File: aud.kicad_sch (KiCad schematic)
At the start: 17 parts, among them J1 AudioJack3_Ground, J3 Conn_01x12_Socket, U1 XTAD5212IRGER

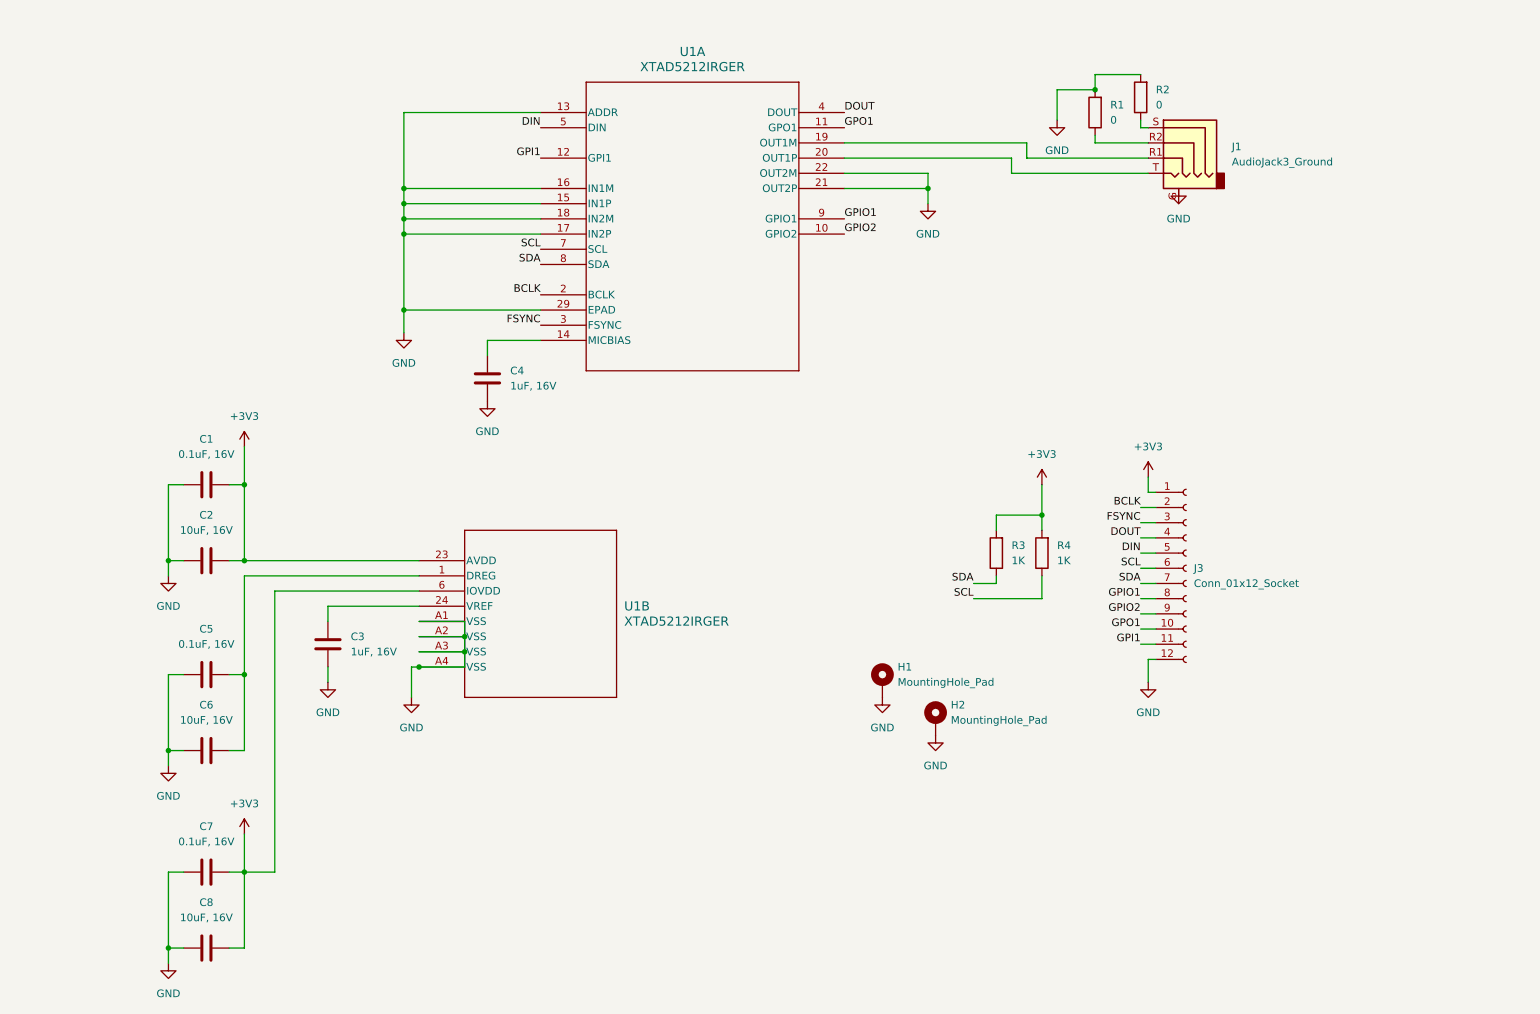
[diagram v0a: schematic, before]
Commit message: Update to version 2
* Fixes the main mistake of not adding AC coupling caps.
* Adds a possibly working MICDET pin.
* Does not break out DOUT anymore.

Signed-off-by: Elvira Khabirova <lineprinter0@gmail.com>
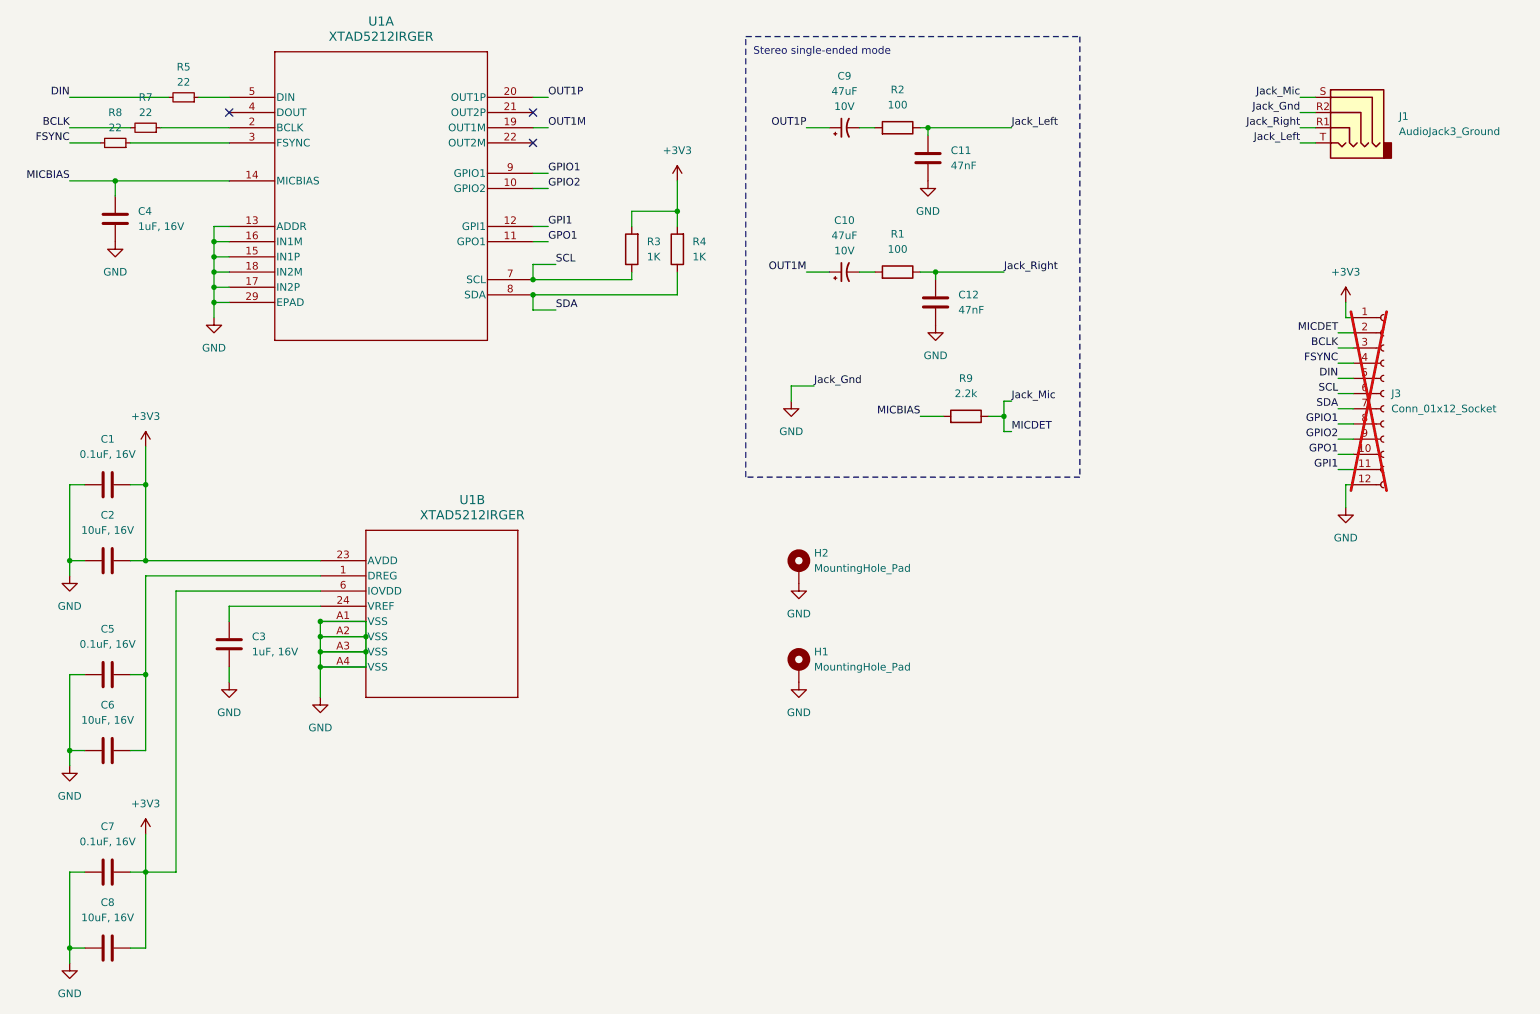
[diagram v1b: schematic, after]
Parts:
- added C10, C9: 47uF, Capacitor_Tantalum_SMD:CP_EIA-3528-21_Kemet-B, symbol PCM_SparkFun-Capacitor:C_Polarized_Small
- added C11, C12: 47nF, Capacitor_SMD:C_0603_1608Metric, symbol Device:C
- added R5, R7, R8: 22, Resistor_SMD:R_0603_1608Metric, symbol Device:R_Small
- added R9: 2.2k, Resistor_SMD:R_0603_1608Metric, symbol Device:R
- C1, C5, C7: footprint Capacitor_SMD:C_0603_1608Metric -> Capacitor_SMD:C_0402_1005Metric
- C2, C6, C8: footprint Capacitor_SMD:C_0603_1608Metric -> Capacitor_SMD:C_0805_2012Metric
- J1: symbol Connector_Audio:AudioJack4_Ground -> Connector_Audio:AudioJack4
- J3: now not fitted
- R1, R2: value 0 -> 100; footprint Resistor_SMD:R_1206_3216Metric -> Resistor_SMD:R_0603_1608Metric; LCSC C17888 -> (none)
- R3, R4: footprint Resistor_SMD:R_0805_2012Metric -> Resistor_SMD:R_0603_1608Metric; LCSC C17513 -> (none)
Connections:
- net BCLK: now also J3.3 (Pin_3), R7.2; no longer J3.2 (Pin_2), U1.2 (BCLK)
- net DIN: now also R5.2; no longer U1.5 (DIN)
- net FSYNC: now also J3.4 (Pin_4), R8.2; no longer J3.3 (Pin_3), U1.3 (FSYNC)
- net GND: now also J1.R2, C11.1, C12.1; no longer R1.2, R2.2, U1.21 (OUT2P), U1.22 (OUT2M)
- net SCL: now also R3.1; no longer R4.1
- net SDA: now also R4.1; no longer R3.1
- net Jack_Right: now reaches R1.1
- net Jack_Right: now also J1.R1, C12.2; no longer J1.R2
- net MICBIAS: now reaches C4.2, U1.14 (MICBIAS)
- net MICBIAS: now also R9.2
- net OUT1M: now reaches U1.19 (OUT1M)
- net OUT1M: now also C10.1; no longer J1.R1
- net Jack_Left: now reaches J1.T
- net Jack_Left: now also R2.1, C11.2; no longer U1.20 (OUT1P)
- net Jack_Mic: now reaches J1.S
- net Jack_Mic: now also J3.2 (Pin_2), R9.1; no longer R2.1
- net DOUT: no longer names the net of U1.4 (DOUT)
- net DOUT: no longer J3.4 (Pin_4)
- new net: R7.1, U1.2 (BCLK)
- new net: R8.1, U1.3 (FSYNC)
- new net: R5.1, U1.5 (DIN)
- new net: C9.2, R2.2
- new net: C10.2, R1.2
- new net OUT1P: C9.1, U1.20 (OUT1P)
- no-connect marks 0 -> 3
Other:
- note added: "Stereo single-ended mode"
- moved on the sheet: C1, C2, C3, C4, C5, C6, C7, C8, H1, H2, R3, R4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
